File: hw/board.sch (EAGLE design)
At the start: 21 parts, among them IC2 HS73XX, IC3 DS1820, IC4 DS1820

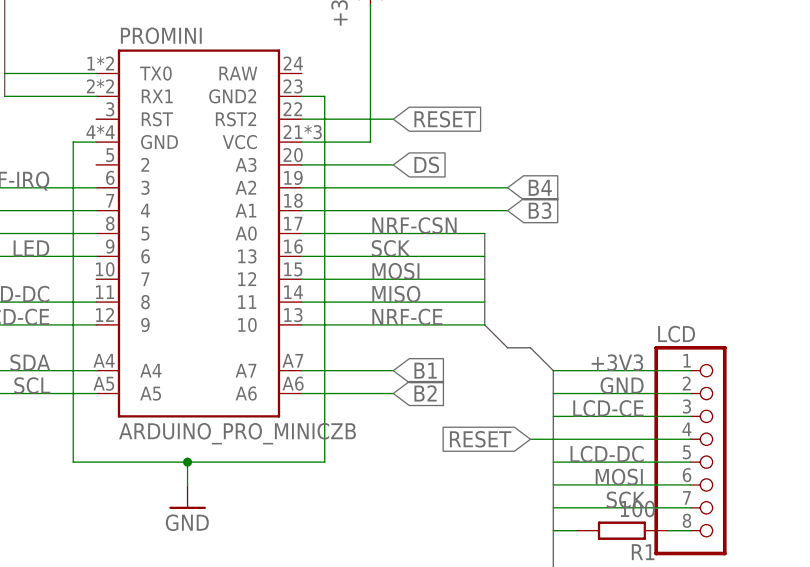
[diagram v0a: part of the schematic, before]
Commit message: Fixed swapped MISO/MOSI in pcb design. -_-
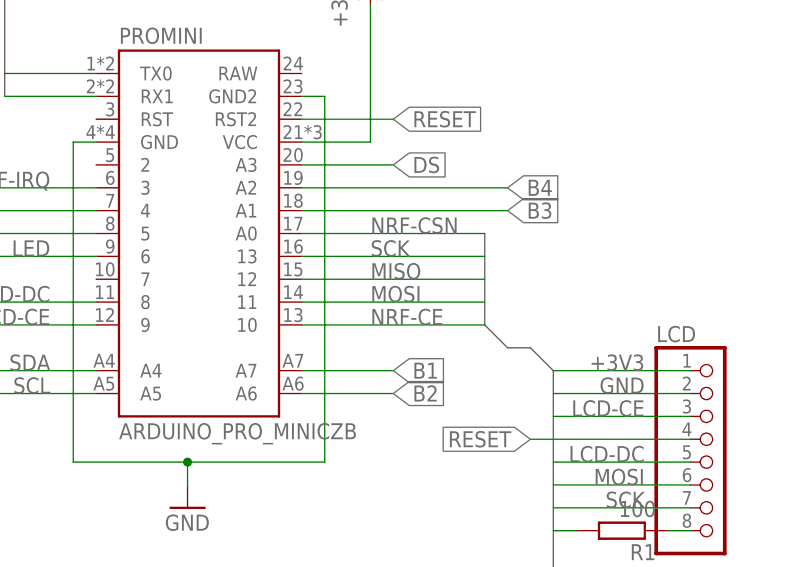
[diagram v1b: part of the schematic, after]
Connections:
- net MISO: now also PROMINI.12; no longer PROMINI.11
- net MOSI: now also PROMINI.11; no longer PROMINI.12
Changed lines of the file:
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@@
 <?xml version="1.0" encoding="utf-8"?>
 <!DOCTYPE eagle SYSTEM "eagle.dtd">
-<eagle version="6.6.0">
+<eagle version="7.2.0">
 <drawing>
 <settings>
@@
 </segment>
 <segment>
+<pinref part="PROMINI" gate="G$1" pin="11"/>
+<wire x1="142.24" y1="88.9" x2="162.56" y2="88.9" width="0.1524" layer="91"/>
+<label x="149.86" y="88.9" size="1.778" layer="95"/>
+</segment>
+</net>
+<net name="SCK" class="0">
+<segment>
+<pinref part="LCD" gate="A" pin="7"/>
+<wire x1="185.42" y1="66.04" x2="170.18" y2="66.04" width="0.1524" layer="91"/>
+<label x="180.34" y="66.04" size="1.778" layer="95" rot="MR0"/>
+</segment>
+<segment>
+<pinref part="NRF24L01" gate="A" pin="5"/>
+<wire x1="185.42" y1="45.72" x2="170.18" y2="45.72" width="0.1524" layer="91"/>
+<label x="180.34" y="45.72" size="1.778" layer="95" rot="MR0"/>
+</segment>
+<segment>
+<pinref part="PROMINI" gate="G$1" pin="13"/>
+<wire x1="142.24" y1="93.98" x2="162.56" y2="93.98" width="0.1524" layer="91"/>
+<label x="149.86" y="93.98" size="1.778" layer="95"/>
+</segment>
+</net>
+<net name="NRF-CE" class="0">
+<segment>
+<pinref part="NRF24L01" gate="A" pin="3"/>
+<wire x1="185.42" y1="48.26" x2="170.18" y2="48.26" width="0.1524" layer="91"/>
+<label x="180.34" y="48.26" size="1.778" layer="95" rot="MR0"/>
+</segment>
+<segment>
+<pinref part="PROMINI" gate="G$1" pin="10"/>
+<wire x1="142.24" y1="86.36" x2="162.56" y2="86.36" width="0.1524" layer="91"/>
+<label x="149.86" y="86.36" size="1.778" layer="95"/>
+</segment>
+</net>
+<net name="NRF-CSN" class="0">
+<segment>
+<pinref part="NRF24L01" gate="A" pin="4"/>
+<wire x1="193.04" y1="48.26" x2="213.36" y2="48.26" width="0.1524" layer="91"/>
+<label x="198.12" y="48.26" size="1.778" layer="95"/>
+</segment>
+<segment>
+<pinref part="PROMINI" gate="G$1" pin="A0"/>
+<wire x1="142.24" y1="96.52" x2="162.56" y2="96.52" width="0.1524" layer="91"/>
+<label x="149.86" y="96.52" size="1.778" layer="95"/>
+</segment>
+</net>
+<net name="MISO" class="0">
+<segment>
+<pinref part="NRF24L01" gate="A" pin="7"/>
+<wire x1="185.42" y1="43.18" x2="170.18" y2="43.18" width="0.1524" layer="91"/>
+<label x="180.34" y="43.18" size="1.778" layer="95" rot="MR0"/>
+</segment>
+<segment>
 <pinref part="PROMINI" gate="G$1" pin="12"/>
 <wire x1="142.24" y1="91.44" x2="162.56" y2="91.44" width="0.1524" layer="91"/>
@@
 </segment>
 </net>
-<net name="SCK" class="0">
-<segment>
-<pinref part="LCD" gate="A" pin="7"/>
-<wire x1="185.42" y1="66.04" x2="170.18" y2="66.04" width="0.1524" layer="91"/>
-<label x="180.34" y="66.04" size="1.778" layer="95" rot="MR0"/>
-</segment>
-<segment>
-<pinref part="NRF24L01" gate="A" pin="5"/>
-<wire x1="185.42" y1="45.72" x2="170.18" y2="45.72" width="0.1524" layer="91"/>
-<label x="180.34" y="45.72" size="1.778" layer="95" rot="MR0"/>
-</segment>
-<segment>
-<pinref part="PROMINI" gate="G$1" pin="13"/>
-<wire x1="142.24" y1="93.98" x2="162.56" y2="93.98" width="0.1524" layer="91"/>
-<label x="149.86" y="93.98" size="1.778" layer="95"/>
-</segment>
-</net>
-<net name="NRF-CE" class="0">
-<segment>
-<pinref part="NRF24L01" gate="A" pin="3"/>
-<wire x1="185.42" y1="48.26" x2="170.18" y2="48.26" width="0.1524" layer="91"/>
-<label x="180.34" y="48.26" size="1.778" layer="95" rot="MR0"/>
-</segment>
-<segment>
-<pinref part="PROMINI" gate="G$1" pin="10"/>
-<wire x1="142.24" y1="86.36" x2="162.56" y2="86.36" width="0.1524" layer="91"/>
-<label x="149.86" y="86.36" size="1.778" layer="95"/>
-</segment>
-</net>
-<net name="NRF-CSN" class="0">
-<segment>
-<pinref part="NRF24L01" gate="A" pin="4"/>
-<wire x1="193.04" y1="48.26" x2="213.36" y2="48.26" width="0.1524" layer="91"/>
-<label x="198.12" y="48.26" size="1.778" layer="95"/>
-</segment>
-<segment>
-<pinref part="PROMINI" gate="G$1" pin="A0"/>
-<wire x1="142.24" y1="96.52" x2="162.56" y2="96.52" width="0.1524" layer="91"/>
-<label x="149.86" y="96.52" size="1.778" layer="95"/>
-</segment>
-</net>
-<net name="MISO" class="0">
-<segment>
-<pinref part="NRF24L01" gate="A" pin="7"/>
-<wire x1="185.42" y1="43.18" x2="170.18" y2="43.18" width="0.1524" layer="91"/>
-<label x="180.34" y="43.18" size="1.778" layer="95" rot="MR0"/>
-</segment>
-<segment>
-<pinref part="PROMINI" gate="G$1" pin="11"/>
-<wire x1="142.24" y1="88.9" x2="162.56" y2="88.9" width="0.1524" layer="91"/>
-<label x="149.86" y="88.9" size="1.778" layer="95"/>
-</segment>
-</net>
